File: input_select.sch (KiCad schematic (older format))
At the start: 9 parts, among them U5 DG509BEQ-T1-E3

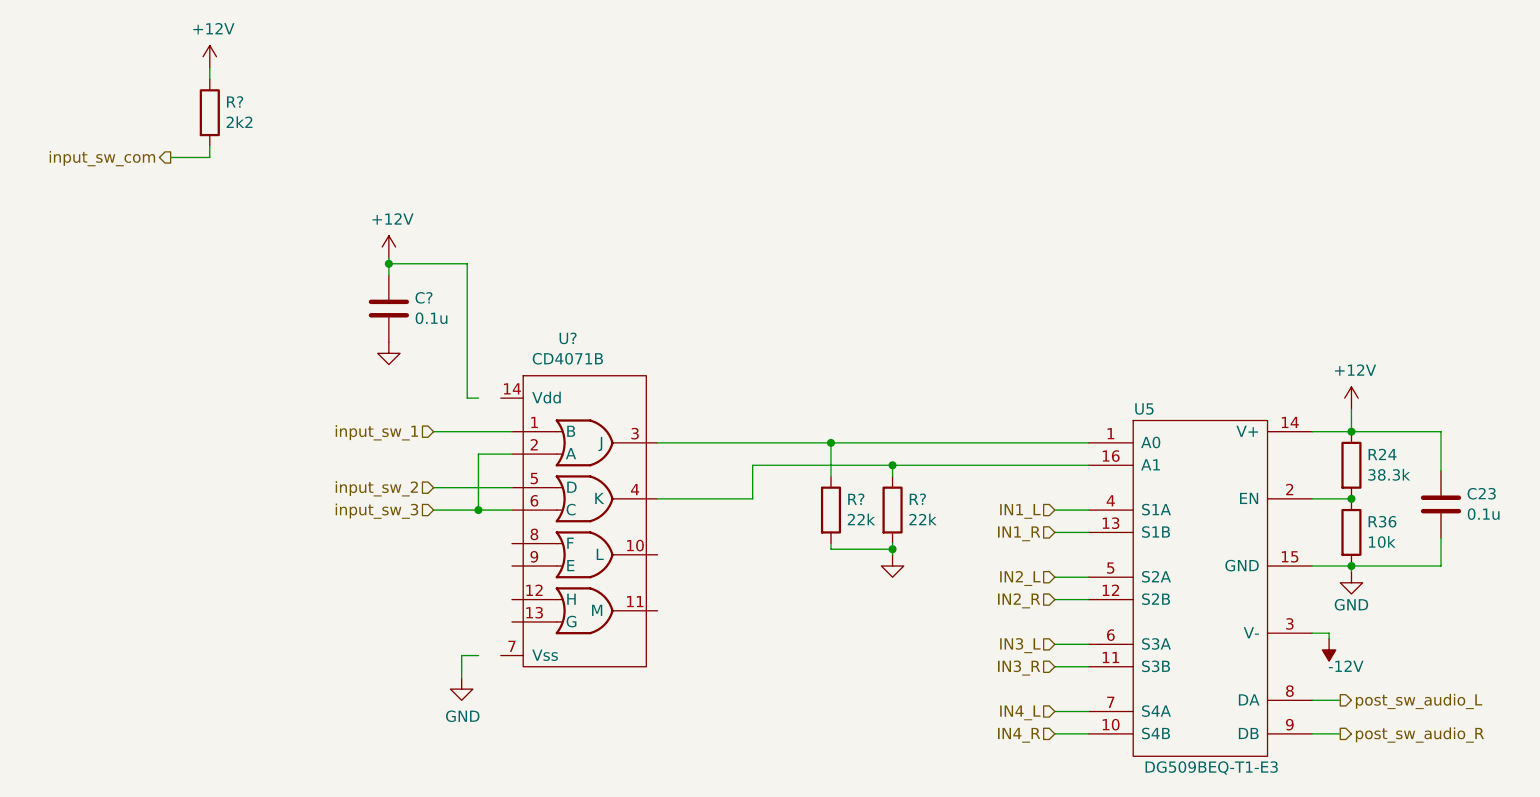
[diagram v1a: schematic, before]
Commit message: Fixed several DRC errors. Tied audoi input returns to GND. Added Switch logic.
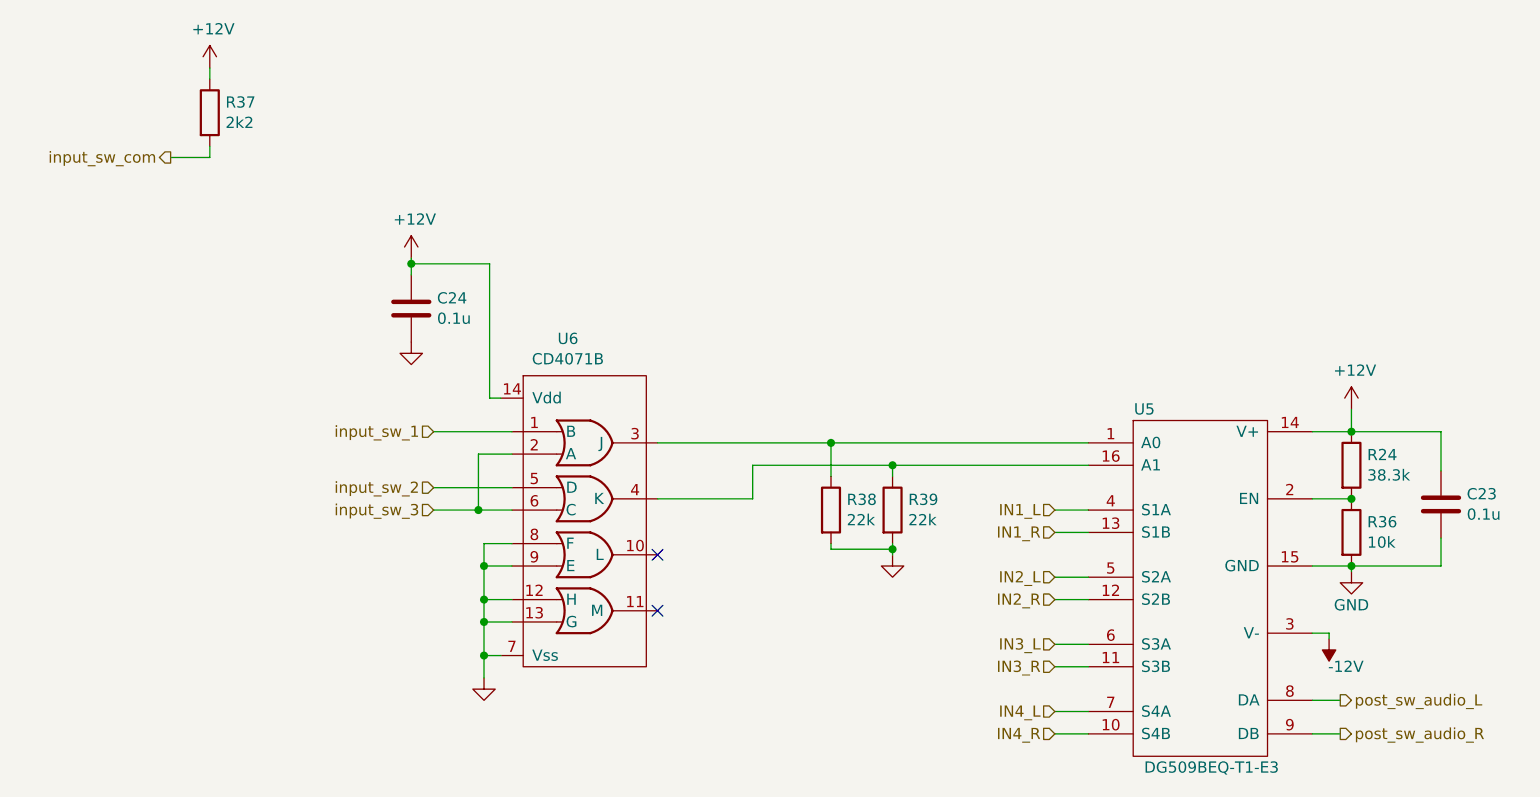
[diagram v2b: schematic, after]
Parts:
- gave numbers to parts that had none: 5
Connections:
- wire segments 49 -> 57
- no-connect marks 0 -> 2
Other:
- moved on the sheet: C24
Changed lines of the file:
@@
 EESchema Schematic File Version 4
+LIBS:AAMB-cache
 EELAYER 30 0
 EELAYER END
@@
 P 1350 800
 AR Path="/5E5C3E1B" Ref="#PWR?"  Part="1"
-AR Path="/5E487042/5E5C3E1B" Ref="#PWR?"  Part="1"
-F 0 "#PWR?" H 1350 650 50  0001 C CNN
+AR Path="/5E487042/5E5C3E1B" Ref="#PWR038"  Part="1"
+F 0 "#PWR038" H 1350 650 50  0001 C CNN
 F 1 "+12V" H 1365 973 50  0000 C CNN
 F 2 "" H 1350 800 50  0001 C CNN
@@
 P 1350 1000
 AR Path="/5E5C3E0E" Ref="R?"  Part="1"
-AR Path="/5E487042/5E5C3E0E" Ref="R?"  Part="1"
-F 0 "R?" H 1420 1046 50  0000 L CNN
+AR Path="/5E487042/5E5C3E0E" Ref="R37"  Part="1"
+F 0 "R37" H 1420 1046 50  0000 L CNN
 F 1 "2k2" H 1420 955 50  0000 L CNN
 F 2 "" V 1280 1000 50  0001 C CNN
@@
 $EndComp
 $Comp
-L audio_amp_custom:CD4071B U?
+L audio_amp_custom:CD4071B U6
 U 1 1 5E5FC527
 P 2550 2325
-F 0 "U?" H 2950 2640 50  0000 C CNN
+F 0 "U6" H 2950 2640 50  0000 C CNN
 F 1 "CD4071B" H 2950 2549 50  0000 C CNN
 F 2 "Package_SO:SOIC-14_3.9x8.7mm_P1.27mm" H 3500 1025 50  0001 C CNN
@@
 $EndComp
 $Comp
-L power:GND #PWR?
-U 1 1 5E5FE2C0
-P 2475 3525
-F 0 "#PWR?" H 2475 3275 50  0001 C CNN
-F 1 "GND" H 2480 3352 50  0000 C CNN
-F 2 "" H 2475 3525 50  0001 C CNN
-F 3 "" H 2475 3525 50  0001 C CNN
-	1    2475 3525
-	1    0    0    -1
-$EndComp
-Wire Wire Line
-	2475 3525 2475 3425
-Wire Wire Line
-	2475 3425 2550 3425
-$Comp
-L Device:C C?
+L Device:C C24
 U 1 1 5E5FEDD7
-P 2150 1875
-F 0 "C?" H 2265 1921 50  0000 L CNN
-F 1 "0.1u" H 2265 1830 50  0000 L CNN
-F 2 "" H 2188 1725 50  0001 C CNN
-F 3 "~" H 2150 1875 50  0001 C CNN
-	1    2150 1875
-	1    0    0    -1
-$EndComp
-$Comp
-L power:GND #PWR?
+P 2250 1875
+F 0 "C24" H 2365 1921 50  0000 L CNN
+F 1 "0.1u" H 2365 1830 50  0000 L CNN
+F 2 "" H 2288 1725 50  0001 C CNN
+F 3 "~" H 2250 1875 50  0001 C CNN
+	1    2250 1875
+	1    0    0    -1
+$EndComp
+$Comp
+L power:GND #PWR040
 U 1 1 5E5FF2BB
-P 2150 2025
-F 0 "#PWR?" H 2150 1775 50  0001 C CNN
-F 1 "GND" H 2250 1925 50  0001 C CNN
-F 2 "" H 2150 2025 50  0001 C CNN
-F 3 "" H 2150 2025 50  0001 C CNN
-	1    2150 2025
-	1    0    0    -1
-$EndComp
-$Comp
-L power:+12V #PWR?
+P 2250 2025
+F 0 "#PWR040" H 2250 1775 50  0001 C CNN
+F 1 "GND" H 2350 1925 50  0001 C CNN
+F 2 "" H 2250 2025 50  0001 C CNN
+F 3 "" H 2250 2025 50  0001 C CNN
+	1    2250 2025
+	1    0    0    -1
+$EndComp
+$Comp
+L power:+12V #PWR039
 U 1 1 5E5FFB0C
-P 2150 1650
-F 0 "#PWR?" H 2150 1500 50  0001 C CNN
-F 1 "+12V" H 2165 1823 50  0000 C CNN
-F 2 "" H 2150 1650 50  0001 C CNN
-F 3 "" H 2150 1650 50  0001 C CNN
-	1    2150 1650
-	1    0    0    -1
-$EndComp
-Wire Wire Line
-	2150 1725 2150 1675
-Wire Wire Line
-	2150 1675 2500 1675
-Wire Wire Line
-	2500 2275 2550 2275
-Connection ~ 2150 1675
-Wire Wire Line
-	2150 1675 2150 1650
-Wire Wire Line
-	2500 1675 2500 2275
-$Comp
-L Device:R R?
+P 2250 1650
+F 0 "#PWR039" H 2250 1500 50  0001 C CNN
+F 1 "+12V" H 2265 1823 50  0000 C CNN
+F 2 "" H 2250 1650 50  0001 C CNN
+F 3 "" H 2250 1650 50  0001 C CNN
+	1    2250 1650
+	1    0    0    -1
+$EndComp
+Wire Wire Line
+	2250 1725 2250 1675
+Wire Wire Line
+	2250 1675 2600 1675
+Wire Wire Line
+	2600 2275 2650 2275
+Connection ~ 2250 1675
+Wire Wire Line
+	2250 1675 2250 1650
+Wire Wire Line
+	2600 1675 2600 2275
+$Comp
+L Device:R R38
 U 1 1 5E60615B
 P 4125 2775
-F 0 "R?" H 4195 2821 50  0000 L CNN
+F 0 "R38" H 4195 2821 50  0000 L CNN
 F 1 "22k" H 4195 2730 50  0000 L CNN
 F 2 "" V 4055 2775 50  0001 C CNN
@@
 $EndComp
 $Comp
-L Device:R R?
+L Device:R R39
 U 1 1 5E60655F
 P 4400 2775
-F 0 "R?" H 4470 2821 50  0000 L CNN
+F 0 "R39" H 4470 2821 50  0000 L CNN
 F 1 "22k" H 4470 2730 50  0000 L CNN
 F 2 "" V 4330 2775 50  0001 C CNN
@@
 $EndComp
 $Comp
-L power:GND #PWR?
+L power:GND #PWR042
 U 1 1 5E6075E4
 P 4400 2975
-F 0 "#PWR?" H 4400 2725 50  0001 C CNN
+F 0 "#PWR042" H 4400 2725 50  0001 C CNN
 F 1 "GND" H 4405 2802 50  0001 C CNN
 F 2 "" H 4400 2975 50  0001 C CNN
@@
 Wire Wire Line
 	2700 2425 2350 2425
+Wire Wire Line
+	2575 3425 2650 3425
+Connection ~ 2575 3425
+Wire Wire Line
+	2575 3275 2575 3425
+Wire Wire Line
+	2700 3275 2575 3275
+Connection ~ 2575 3275
+Connection ~ 2575 3175
+Wire Wire Line
+	2700 3175 2575 3175
+Wire Wire Line
+	2575 3175 2575 3275
+Wire Wire Line
+	2575 3025 2575 3175
+Wire Wire Line
+	2700 3025 2575 3025
+Connection ~ 2575 3025
+Wire Wire Line
+	2700 2925 2575 2925
+Wire Wire Line
+	2575 2925 2575 3025
+Wire Wire Line
+	2575 3525 2575 3425
+$Comp
+L power:GND #PWR041
+U 1 1 5E5FE2C0
+P 2575 3525
+F 0 "#PWR041" H 2575 3275 50  0001 C CNN
+F 1 "GND" H 2580 3352 50  0001 C CNN
+F 2 "" H 2575 3525 50  0001 C CNN
+F 3 "" H 2575 3525 50  0001 C CNN
+	1    2575 3525
+	1    0    0    -1
+$EndComp
+NoConn ~ 3350 3225
+NoConn ~ 3350 2975
 $EndSCHEMATC

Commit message: Schecmatic cleanup.
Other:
- moved on the sheet: R37
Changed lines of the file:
@@
 L power:+12V #PWR?
 U 1 1 5E5C3E1B
-P 1350 800
+P 1525 1700
 AR Path="/5E5C3E1B" Ref="#PWR?"  Part="1"
 AR Path="/5E487042/5E5C3E1B" Ref="#PWR038"  Part="1"
-F 0 "#PWR038" H 1350 650 50  0001 C CNN
-F 1 "+12V" H 1365 973 50  0000 C CNN
-F 2 "" H 1350 800 50  0001 C CNN
-F 3 "" H 1350 800 50  0001 C CNN
-	1    1350 800
+F 0 "#PWR038" H 1525 1550 50  0001 C CNN
+F 1 "+12V" H 1540 1873 50  0000 C CNN
+F 2 "" H 1525 1700 50  0001 C CNN
+F 3 "" H 1525 1700 50  0001 C CNN
+	1    1525 1700
 	1    0    0    -1
 $EndComp
 Wire Wire Line
-	1350 850  1350 800
+	1525 1750 1525 1700
 Wire Wire Line
-	1350 1150 1350 1200
-Text HLabel 1175 1200 0    50   Output ~ 0
+	1525 2050 1525 2100
+Text HLabel 1350 2100 0    50   Output ~ 0
 input_sw_com
 Wire Wire Line
-	1175 1200 1350 1200
+	1350 2100 1525 2100
 $Comp
 L Device:R R?
 U 1 1 5E5C3E0E
-P 1350 1000
+P 1525 1900
 AR Path="/5E5C3E0E" Ref="R?"  Part="1"
 AR Path="/5E487042/5E5C3E0E" Ref="R37"  Part="1"
-F 0 "R37" H 1420 1046 50  0000 L CNN
-F 1 "2k2" H 1420 955 50  0000 L CNN
-F 2 "" V 1280 1000 50  0001 C CNN
-F 3 "~" H 1350 1000 50  0001 C CNN
-	1    1350 1000
+F 0 "R37" H 1595 1946 50  0000 L CNN
+F 1 "2k2" H 1595 1855 50  0000 L CNN
+F 2 "" V 1455 1900 50  0001 C CNN
+F 3 "~" H 1525 1900 50  0001 C CNN
+	1    1525 1900
 	1    0    0    -1
 $EndComp

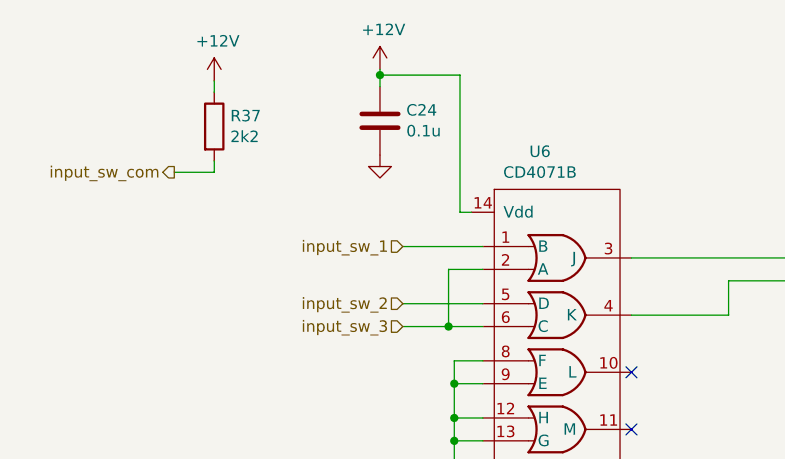
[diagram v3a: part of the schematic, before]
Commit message: Added test points. Schematic cleanup.
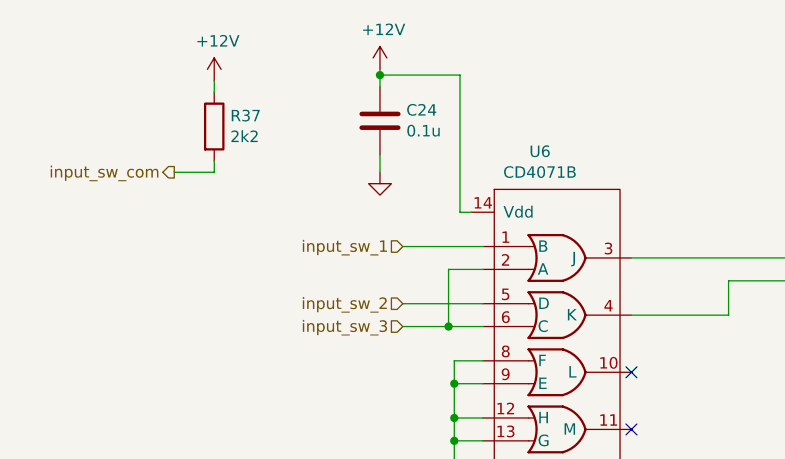
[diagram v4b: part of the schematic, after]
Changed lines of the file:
@@
 $Descr A4 11693 8268
 encoding utf-8
-Sheet 6 6
+Sheet 5 6
 Title ""
 Date ""
@@
 L power:GND #PWR040
 U 1 1 5E5FF2BB
-P 2250 2025
-F 0 "#PWR040" H 2250 1775 50  0001 C CNN
-F 1 "GND" H 2350 1925 50  0001 C CNN
-F 2 "" H 2250 2025 50  0001 C CNN
-F 3 "" H 2250 2025 50  0001 C CNN
-	1    2250 2025
+P 2250 2100
+F 0 "#PWR040" H 2250 1850 50  0001 C CNN
+F 1 "GND" H 2350 2000 50  0001 C CNN
+F 2 "" H 2250 2100 50  0001 C CNN
+F 3 "" H 2250 2100 50  0001 C CNN
+	1    2250 2100
 	1    0    0    -1
 $EndComp
@@
 NoConn ~ 3350 3225
 NoConn ~ 3350 2975
+Wire Wire Line
+	2250 2100 2250 2025
 $EndSCHEMATC

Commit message: Cleaning up user configs.
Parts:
- C23, C24: footprint (none) -> Capacitor_SMD:C_0603_1608Metric_Pad1.05x0.95mm_HandSolder; DigiKey (none) -> https://www.digikey.com/product-detail/en/kemet/C0603C104Z3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
- R37, R38, R39: footprint (none) -> Resistor_SMD:R_0603_1608Metric_Pad1.05x0.95mm_HandSolder
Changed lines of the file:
@@
 	6275 2725 6450 2725
 Connection ~ 6450 2725
-$Comp
-L Device:C C23
-U 1 1 5E49B618
-P 6850 2750
-F 0 "C23" H 6965 2796 50  0000 L CNN
-F 1 "0.1u" H 6965 2705 50  0000 L CNN
-F 2 "" H 6888 2600 50  0001 C CNN
-F 3 "~" H 6850 2750 50  0001 C CNN
-	1    6850 2750
-	1    0    0    -1
-$EndComp
 Wire Wire Line
 	6850 2600 6850 2425
@@
 F 0 "R37" H 1595 1946 50  0000 L CNN
 F 1 "2k2" H 1595 1855 50  0000 L CNN
-F 2 "" V 1455 1900 50  0001 C CNN
+F 2 "Resistor_SMD:R_0603_1608Metric_Pad1.05x0.95mm_HandSolder" V 1455 1900 50  0001 C CNN
 F 3 "~" H 1525 1900 50  0001 C CNN
 	1    1525 1900
@@
 $EndComp
 $Comp
-L Device:C C24
-U 1 1 5E5FEDD7
-P 2250 1875
-F 0 "C24" H 2365 1921 50  0000 L CNN
-F 1 "0.1u" H 2365 1830 50  0000 L CNN
-F 2 "" H 2288 1725 50  0001 C CNN
-F 3 "~" H 2250 1875 50  0001 C CNN
-	1    2250 1875
-	1    0    0    -1
-$EndComp
-$Comp
 L power:GND #PWR040
 U 1 1 5E5FF2BB
@@
 F 0 "R38" H 4195 2821 50  0000 L CNN
 F 1 "22k" H 4195 2730 50  0000 L CNN
-F 2 "" V 4055 2775 50  0001 C CNN
+F 2 "Resistor_SMD:R_0603_1608Metric_Pad1.05x0.95mm_HandSolder" V 4055 2775 50  0001 C CNN
 F 3 "~" H 4125 2775 50  0001 C CNN
 	1    4125 2775
@@
 F 0 "R39" H 4470 2821 50  0000 L CNN
 F 1 "22k" H 4470 2730 50  0000 L CNN
-F 2 "" V 4330 2775 50  0001 C CNN
+F 2 "Resistor_SMD:R_0603_1608Metric_Pad1.05x0.95mm_HandSolder" V 4330 2775 50  0001 C CNN
 F 3 "~" H 4400 2775 50  0001 C CNN
 	1    4400 2775
@@
 Wire Wire Line
 	2250 2100 2250 2025
+$Comp
+L Device:C C?
+U 1 1 5E6A0445
+P 2250 1875
+AR Path="/5E227FCE/5E6A0445" Ref="C?"  Part="1"
+AR Path="/5E487042/5E6A0445" Ref="C23"  Part="1"
+F 0 "C23" H 2365 1921 50  0000 L CNN
+F 1 "0.1u" H 2365 1830 50  0000 L CNN
+F 2 "Capacitor_SMD:C_0603_1608Metric_Pad1.05x0.95mm_HandSolder" H 2288 1725 50  0001 C CNN
+F 3 "https://api.kemet.com/component-edge/download/datasheet/C0603C104Z3VACTU.pdf" H 2250 1875 50  0001 C CNN
+F 4 "https://www.digikey.com/product-detail/en/kemet/C0603C104Z3VACTU/399-1100-1-ND/411375" H 2250 1875 50  0001 C CNN "DigiKey"
+	1    2250 1875
+	1    0    0    -1
+$EndComp
+$Comp
+L Device:C C?
+U 1 1 5E6A15C2
+P 6850 2750
+AR Path="/5E227FCE/5E6A15C2" Ref="C?"  Part="1"
+AR Path="/5E487042/5E6A15C2" Ref="C24"  Part="1"
+F 0 "C24" H 6965 2796 50  0000 L CNN
+F 1 "0.1u" H 6965 2705 50  0000 L CNN
+F 2 "Capacitor_SMD:C_0603_1608Metric_Pad1.05x0.95mm_HandSolder" H 6888 2600 50  0001 C CNN
+F 3 "https://api.kemet.com/component-edge/download/datasheet/C0603C104Z3VACTU.pdf" H 6850 2750 50  0001 C CNN
+F 4 "https://www.digikey.com/product-detail/en/kemet/C0603C104Z3VACTU/399-1100-1-ND/411375" H 6850 2750 50  0001 C CNN "DigiKey"
+	1    6850 2750
+	1    0    0    -1
+$EndComp
 $EndSCHEMATC

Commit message: Lots of part changes to SMD devices. Adding MPN, MFG to all parts for BOM export.
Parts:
- C23, C24: MFG (none) -> KEMET; MPN (none) -> C0603C104Z3VACTU
- U5: MFG (none) -> Vishay Siliconix; MPN (none) -> DG509BEQ-T1-E3
- U6: MFG (none) -> Texas Instruments; MPN (none) -> CD4071BM96
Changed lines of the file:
@@
 F 3 "http://www.vishay.com/docs/64821/dg508b.pdf" H 5775 3025 50  0001 C CNN
 F 4 "https://www.digikey.com/product-detail/en/vishay-siliconix/DG509BEQ-T1-E3/DG509BEQ-T1-E3CT-ND/2296900" H 7075 1925 50  0001 C CNN "DigiKey"
+F 5 "Vishay Siliconix" H 5775 3025 50  0001 C CNN "MFG"
+F 6 "DG509BEQ-T1-E3" H 5775 3025 50  0001 C CNN "MPN"
 	1    5775 3025
 	1    0    0    -1
@@
 F 3 "http://www.ti.com/general/docs/suppproductinfo.tsp?distId=10&gotoUrl=http%3A%2F%2Fwww.ti.com%2Flit%2Fgpn%2Fcd4071b" H 1300 2075 50  0001 C CNN
 F 4 "https://www.digikey.com/product-detail/en/texas-instruments/CD4071BM96/296-25953-1-ND/2254806" H 4650 925 50  0001 C CNN "DigiKey"
+F 5 "Texas Instruments" H 2550 2325 50  0001 C CNN "MFG"
+F 6 "CD4071BM96" H 2550 2325 50  0001 C CNN "MPN"
 	1    2550 2325
 	1    0    0    -1
@@
 F 3 "https://api.kemet.com/component-edge/download/datasheet/C0603C104Z3VACTU.pdf" H 2250 1875 50  0001 C CNN
 F 4 "https://www.digikey.com/product-detail/en/kemet/C0603C104Z3VACTU/399-1100-1-ND/411375" H 2250 1875 50  0001 C CNN "DigiKey"
+F 5 "KEMET" H 2250 1875 50  0001 C CNN "MFG"
+F 6 "C0603C104Z3VACTU" H 2250 1875 50  0001 C CNN "MPN"
 	1    2250 1875
 	1    0    0    -1
@@
 F 3 "https://api.kemet.com/component-edge/download/datasheet/C0603C104Z3VACTU.pdf" H 6850 2750 50  0001 C CNN
 F 4 "https://www.digikey.com/product-detail/en/kemet/C0603C104Z3VACTU/399-1100-1-ND/411375" H 6850 2750 50  0001 C CNN "DigiKey"
+F 5 "KEMET" H 6850 2750 50  0001 C CNN "MFG"
+F 6 "C0603C104Z3VACTU" H 6850 2750 50  0001 C CNN "MPN"
 	1    6850 2750
 	1    0    0    -1
